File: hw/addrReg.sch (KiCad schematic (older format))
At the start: 6 parts

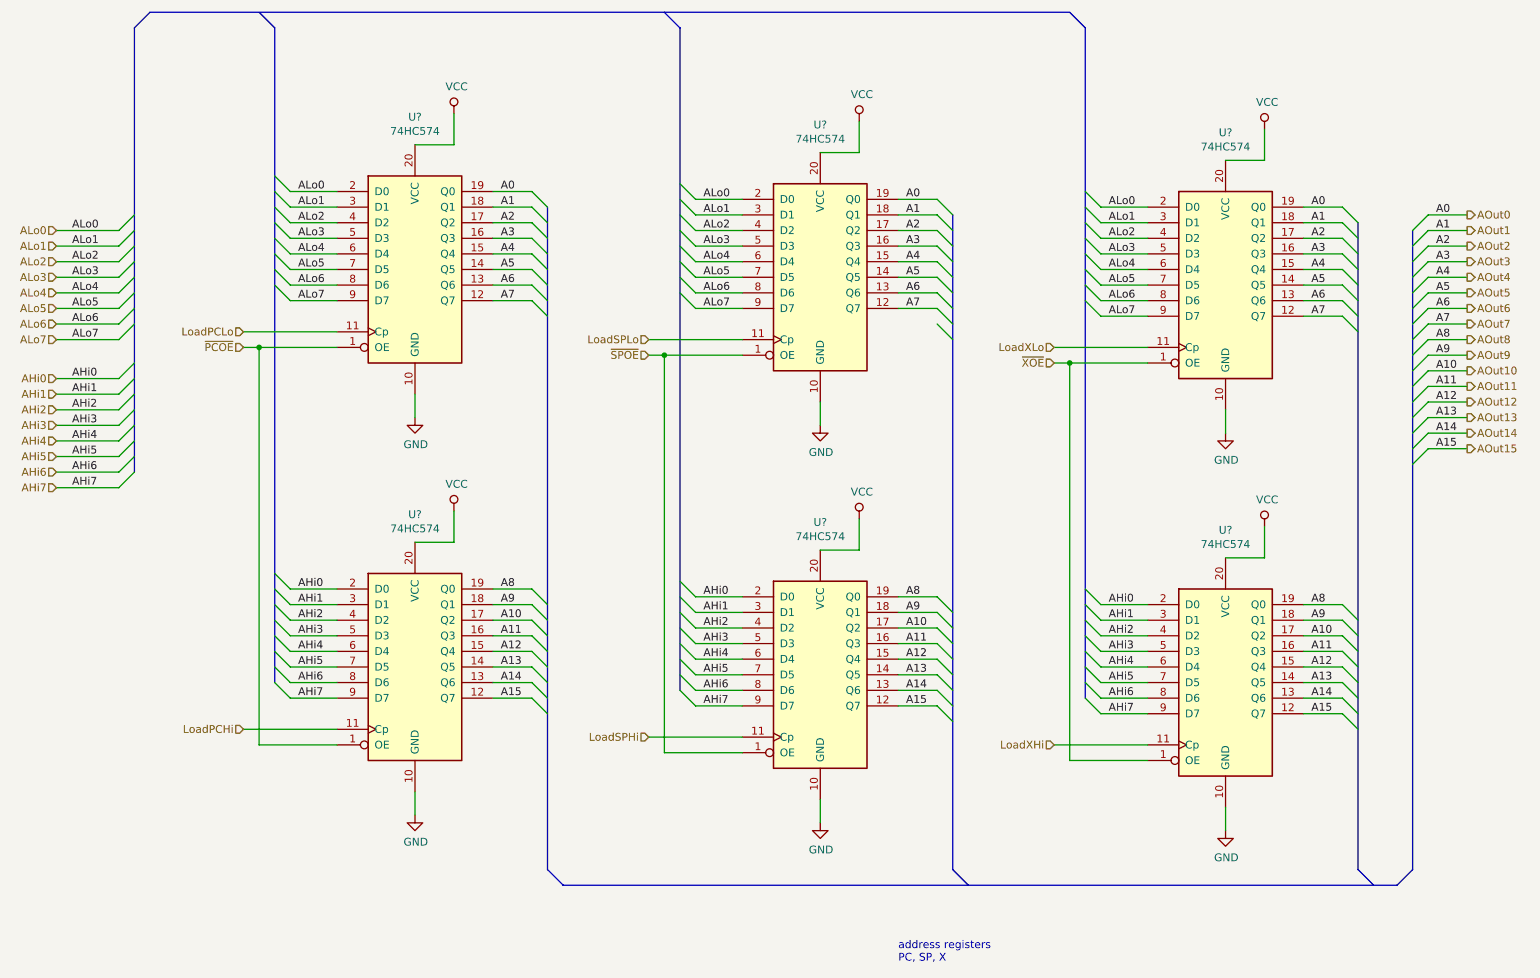
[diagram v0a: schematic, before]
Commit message: address registers have only one load input
Both bytes of the address will always be loaded
at the same time.

Also did a few cleanups of the addrReg schematic.
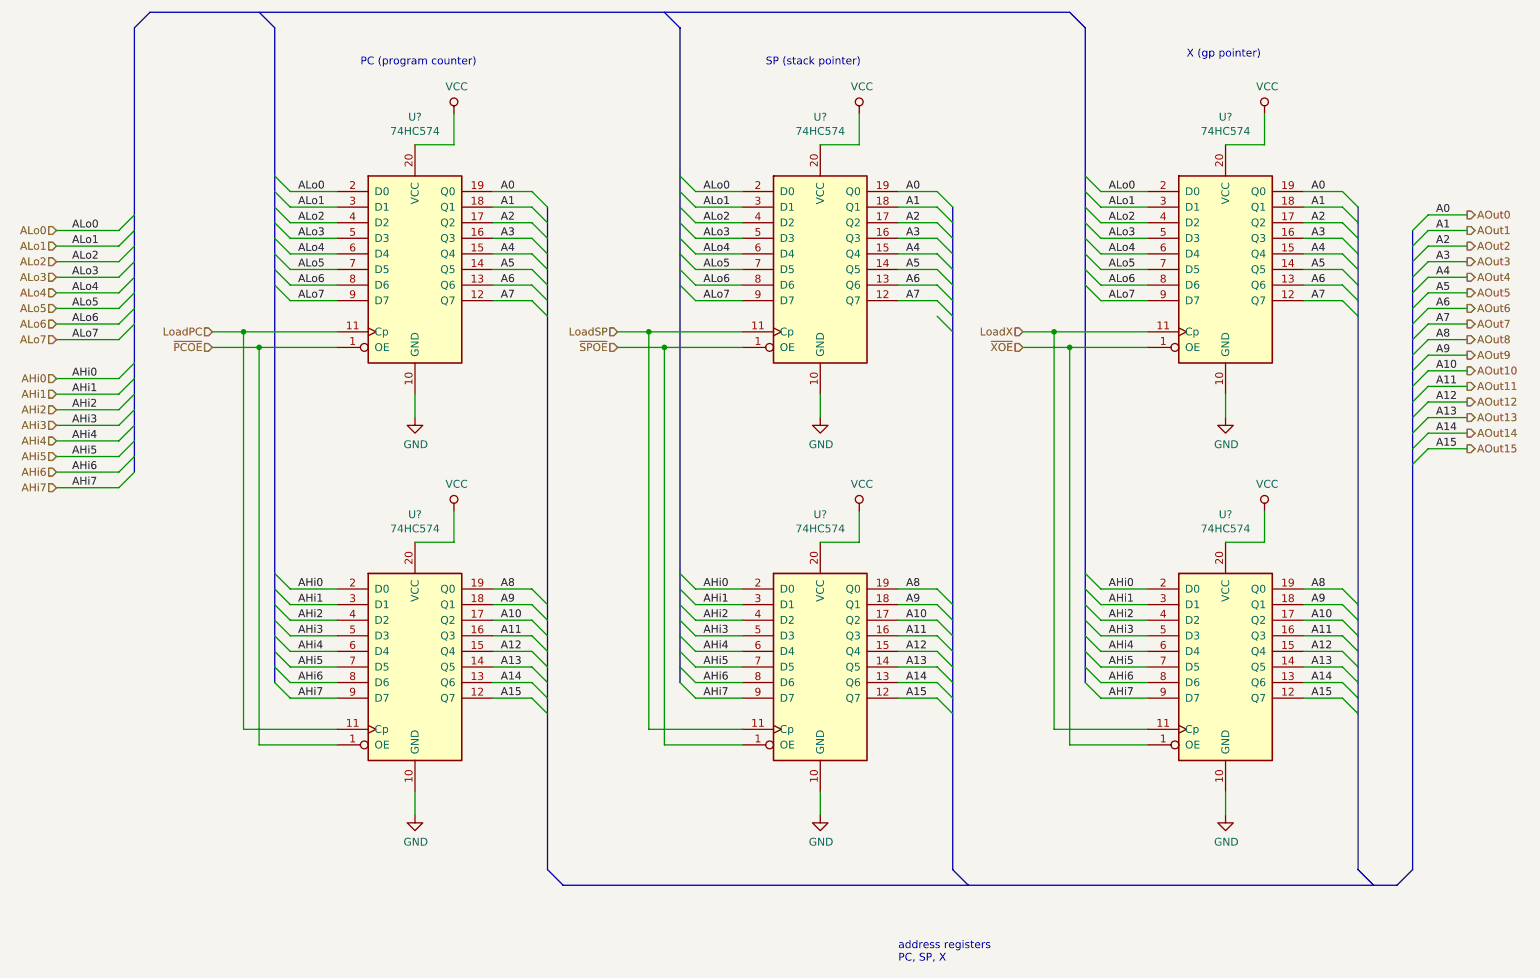
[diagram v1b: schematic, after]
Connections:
- net LoadPCLo is gone; now on net LoadPC: U?.11 (Cp)
- net LoadSPLo is gone; now on net LoadSP: U?.11 (Cp)
- net LoadXLo is gone; now on net LoadX: U?.11 (Cp)
- net LoadPCHi renamed LoadPC
- net LoadSPHi renamed LoadSP
- net LoadXHi renamed LoadX
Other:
- note added: "PC (program counter)"
- note added: "SP (stack pointer)"
- note added: "X (gp pointer)"
- moved on the sheet: U?
